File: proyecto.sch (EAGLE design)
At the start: 48 parts, among them IC1 ADE9153AACPZ, J1 796638-3, K1 PR28-3V-360-1A-E, Q1 12.288M, Q2 BSS123, U1 ESP32-PICO-MINI-02-N8R2ESP32-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

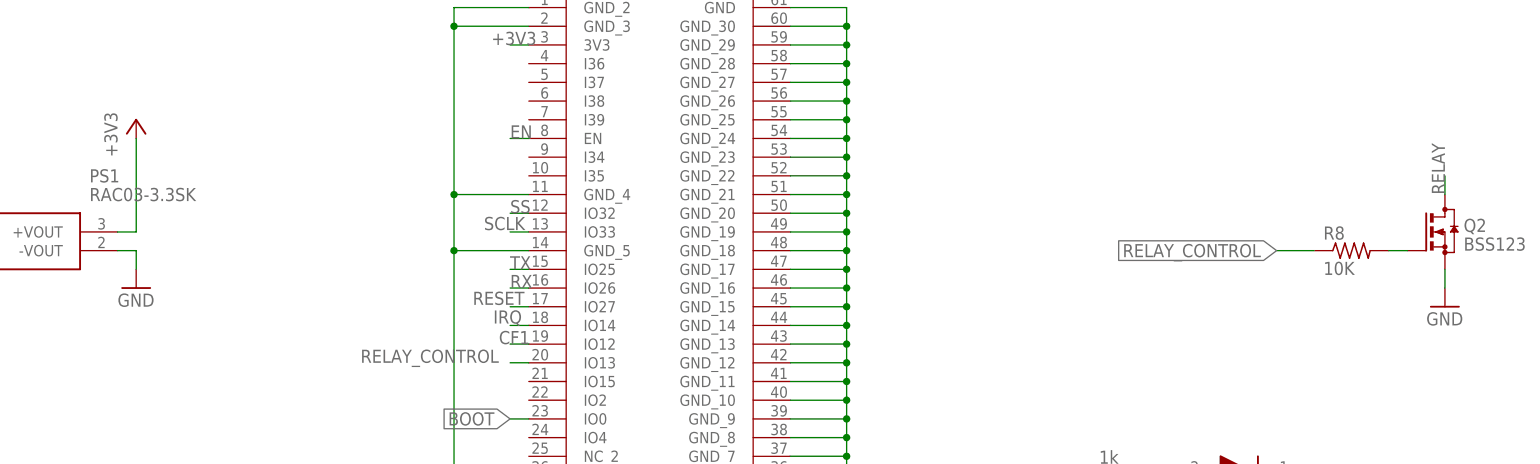
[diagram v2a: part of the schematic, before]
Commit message: Se añadieron test pads
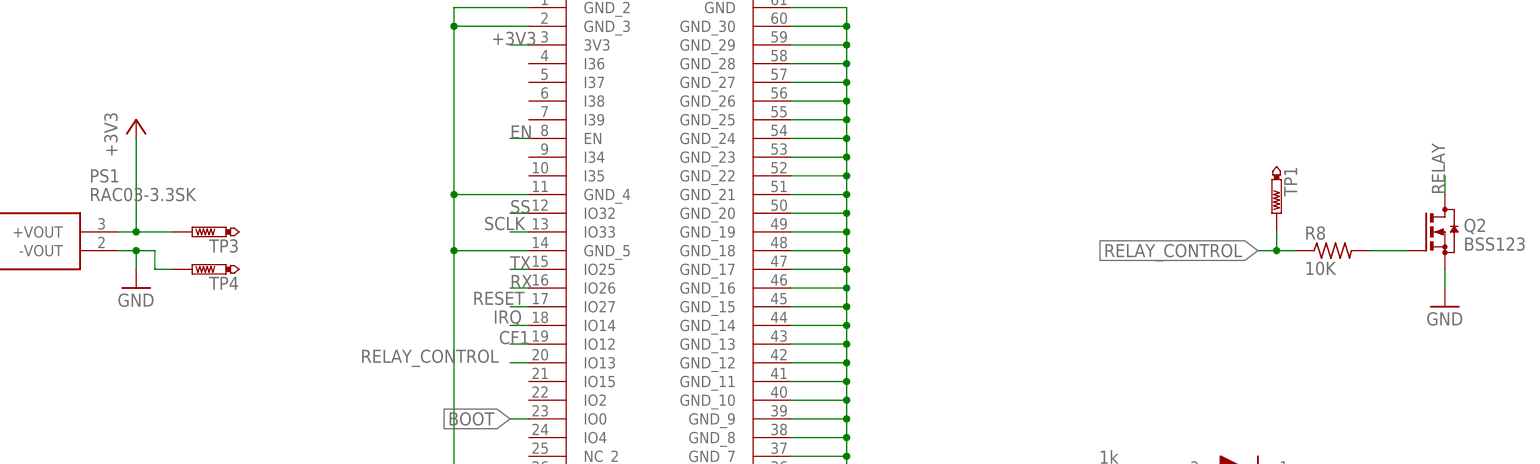
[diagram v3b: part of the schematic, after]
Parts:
- added TP1, TP3, TP4: PTR1TP10R, testpad:PTR1TP10R
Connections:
- net +3V3: now also TP3.TP
- net GND: now also TP4.TP
- net RELAY_CONTROL: now also TP1.TP
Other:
- moved on the sheet: R8
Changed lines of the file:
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@@
 <part name="LED3" library="libreria_propia" deviceset="NCD0805G1" device=""/>
 <part name="R12" library="rcl" library_urn="urn:adsk.eagle:library:334" deviceset="R-US_" device="R0402" package3d_urn="urn:adsk.eagle:package:23547/3" value="1k"/>
+<part name="TP3" library="testpad" library_urn="urn:adsk.eagle:library:385" deviceset="PTR1" device="TP10R" package3d_urn="urn:adsk.eagle:package:27959/1" value="PTR1TP10R"/>
+<part name="TP4" library="testpad" library_urn="urn:adsk.eagle:library:385" deviceset="PTR1" device="TP10R" package3d_urn="urn:adsk.eagle:package:27959/1" value="PTR1TP10R"/>
+<part name="TP1" library="testpad" library_urn="urn:adsk.eagle:library:385" deviceset="PTR1" device="TP10R" package3d_urn="urn:adsk.eagle:package:27959/1"/>
 </parts>
 <sheets>
@@
 <attribute name="VALUE" x="233.68" y="99.06" size="1.778" layer="96"/>
 </instance>
-<instance part="R8" gate="G$1" x="223.52" y="109.22" smashed="yes">
-<attribute name="NAME" x="219.71" y="110.7186" size="1.778" layer="95"/>
-<attribute name="VALUE" x="219.71" y="105.918" size="1.778" layer="96"/>
+<instance part="R8" gate="G$1" x="220.98" y="109.22" smashed="yes">
+<attribute name="NAME" x="217.17" y="110.7186" size="1.778" layer="95"/>
+<attribute name="VALUE" x="217.17" y="105.918" size="1.778" layer="96"/>
 </instance>
 <instance part="C23" gate="G$1" x="38.1" y="14.224" smashed="yes">
@@
 <attribute name="NAME" x="189.23" y="77.2414" size="1.778" layer="95" rot="MR180"/>
 <attribute name="VALUE" x="189.23" y="82.042" size="1.778" layer="96" rot="MR180"/>
+</instance>
+<instance part="TP3" gate="G$1" x="66.04" y="111.76" smashed="yes" rot="R90">
+<attribute name="NAME" x="72.39" y="110.744" size="1.778" layer="95" rot="R180"/>
+<attribute name="TP_SIGNAL_NAME" x="68.58" y="113.03" size="1.778" layer="97" rot="R90"/>
+</instance>
+<instance part="TP4" gate="G$1" x="66.04" y="106.68" smashed="yes" rot="R90">
+<attribute name="NAME" x="72.39" y="105.664" size="1.778" layer="95" rot="R180"/>
+<attribute name="TP_SIGNAL_NAME" x="68.58" y="107.95" size="1.778" layer="97" rot="R90"/>
+</instance>
+<instance part="TP1" gate="G$1" x="213.36" y="114.3" smashed="yes" rot="R180">
+<attribute name="NAME" x="214.376" y="120.65" size="1.778" layer="95" rot="R270"/>
+<attribute name="TP_SIGNAL_NAME" x="212.09" y="116.84" size="1.778" layer="97" rot="R180"/>
 </instance>
 </instances>
@@
 <pinref part="GND12" gate="1" pin="GND"/>
 <wire x1="58.42" y1="106.68" x2="58.42" y2="109.22" width="0.1524" layer="91"/>
+<pinref part="TP4" gate="G$1" pin="TP"/>
+<wire x1="63.5" y1="106.68" x2="60.96" y2="106.68" width="0.1524" layer="91"/>
+<wire x1="60.96" y1="106.68" x2="60.96" y2="109.22" width="0.1524" layer="91"/>
+<wire x1="60.96" y1="109.22" x2="58.42" y2="109.22" width="0.1524" layer="91"/>
+<junction x="58.42" y="109.22"/>
 </segment>
 </net>
@@
 <pinref part="+3V1" gate="G$1" pin="+3V3"/>
 <wire x1="58.42" y1="111.76" x2="58.42" y2="124.46" width="0.1524" layer="91"/>
+<pinref part="TP3" gate="G$1" pin="TP"/>
+<wire x1="63.5" y1="111.76" x2="58.42" y2="111.76" width="0.1524" layer="91"/>
+<junction x="58.42" y="111.76"/>
 </segment>
 <segment>
@@
 </segment>
 </net>
-<net name="N$13" class="0">
-<segment>
-<pinref part="R8" gate="G$1" pin="2"/>
-<pinref part="Q2" gate="G$1" pin="G"/>
-<wire x1="228.6" y1="109.22" x2="231.14" y2="109.22" width="0.1524" layer="91"/>
-</segment>
-</net>
 <net name="RELAY_CONTROL" class="0">
 <segment>
 <pinref part="R8" gate="G$1" pin="1"/>
-<label x="213.36" y="109.22" size="1.778" layer="95" rot="R180" xref="yes"/>
-<wire x1="218.44" y1="109.22" x2="213.36" y2="109.22" width="0.1524" layer="91"/>
+<label x="210.82" y="109.22" size="1.778" layer="95" rot="R180" xref="yes"/>
+<wire x1="215.9" y1="109.22" x2="213.36" y2="109.22" width="0.1524" layer="91"/>
+<pinref part="TP1" gate="G$1" pin="TP"/>
+<wire x1="213.36" y1="109.22" x2="210.82" y2="109.22" width="0.1524" layer="91"/>
+<wire x1="213.36" y1="111.76" x2="213.36" y2="109.22" width="0.1524" layer="91"/>
+<junction x="213.36" y="109.22"/>
 </segment>
 <segment>
@@
 </segment>
 </net>
+<net name="N$13" class="0">
+<segment>
+<pinref part="R8" gate="G$1" pin="2"/>
+<pinref part="Q2" gate="G$1" pin="G"/>
+<wire x1="226.06" y1="109.22" x2="231.14" y2="109.22" width="0.1524" layer="91"/>
+</segment>
+</net>

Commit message: Finalizado
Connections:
- net MONDA renamed CARGA-M
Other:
- note added: "1/2"
- note added: "2/2"
- note added: "CIRCUITO DE POTENCIA EN ESTA PARTE SE UBICA EL MEDIDOR DE ENERGIA CON SU CIRCUITO ESPECIFICADO EN EL DATASHEET, TAMBIEN ESTA EL RELE DEL CONTROL DE LA CARGA Y LA BORNERA HACIA LA CARGA"
- note added: "JUAN ANDRES ABELLA BALLEN"
- note added: "JUAN ANDRES RODRIGUEZ RUIZ"
- note added: "MEDIDOR DE VARIABLES ELECTRICAS"
- note added: "PARTE DE BAJA POTENCIA EN ESTA PARTE ESTA EL CIRCUITO DEL MICROCONTROLADOR, FUENTE DE PODER Y EL SISTEMA DE CONTROL DE RELE"
- note added: "PROYECTO IDIE"
- note added: "TOMAS FELIPE MONTAÑEZ PIÑEROS"
- note removed: "1.0"
- note removed: "LOS MAS ASPEROS"
- moved on the sheet: C17, C18, C19, C20, C21, C22, C23, D1, IC1, J1, K1, LED1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

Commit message: Adicion de pistas faltantes
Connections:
- new net CF2: IC1.ZX/DREADY/CF2, U1.IO13
- new net N$16: IC1.IBN, IC1.IBP
- net GND: now also IC1.IBMS
- net N$2: now also IC1.IAMS
- net RELAY_CONTROL: now also U1.IO15; no longer U1.IO13

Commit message: .
.
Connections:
- net CARGA renamed M
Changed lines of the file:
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@@
 </segment>
 </net>
-<net name="CARGA" class="0">
+<net name="M" class="0">
 <segment>
 <pinref part="J1" gate="G$1" pin="1"/>

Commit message: XDIN
XDIN
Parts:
- removed Q1: 12.288M, crystal-geyer_V1_0:KX-5
- added Y1: NX3225GA-12.288M-STD-CRG-2, SamacSys_Parts:NX3225GA-12.288M-STD-CRG-2
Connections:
- net CLKIN: now also Y1.CRYSTAL_1; no longer Q1.1
- net CLKOUT: now also Y1.CRYSTAL_2; no longer Q1.2
- net GND: now also Y1.GND_1, Y1.GND_2
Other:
- moved on the sheet: C15, C16
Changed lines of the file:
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@@
 <part name="C12" library="rcl" library_urn="urn:adsk.eagle:library:334" deviceset="C-EU" device="C0402K" package3d_urn="urn:adsk.eagle:package:23679/2" value="4.7u"/>
 <part name="GND9" library="supply1" library_urn="urn:adsk.eagle:library:371" deviceset="GND" device=""/>
-<part name="Q1" library="crystal-geyer_V1_0" library_urn="urn:adsk.eagle:library:203" deviceset="KX" device="-5" package3d_urn="urn:adsk.eagle:package:11926/1" value="12.288M"/>
 <part name="C13" library="rcl" library_urn="urn:adsk.eagle:library:334" deviceset="C-EU" device="C0402K" package3d_urn="urn:adsk.eagle:package:23679/2" value="0.1u"/>
 <part name="C14" library="rcl" library_urn="urn:adsk.eagle:library:334" deviceset="C-EU" device="C0402K" package3d_urn="urn:adsk.eagle:package:23679/2" value="4.7u"/>
@@
 <part name="TP4" library="testpad" library_urn="urn:adsk.eagle:library:385" deviceset="PTR1" device="TP10R" package3d_urn="urn:adsk.eagle:package:27959/1" value="PTR1TP10R"/>
 <part name="TP1" library="testpad" library_urn="urn:adsk.eagle:library:385" deviceset="PTR1" device="TP10R" package3d_urn="urn:adsk.eagle:package:27959/1"/>
+<part name="Y1" library="SamacSys_Parts" deviceset="NX3225GA-12.288M-STD-CRG-2" device=""/>
+<part name="GND20" library="supply1" library_urn="urn:adsk.eagle:library:371" deviceset="GND" device=""/>
+<part name="GND21" library="supply1" library_urn="urn:adsk.eagle:library:371" deviceset="GND" device=""/>
 </parts>
 <sheets>
@@
 <attribute name="VALUE" x="332.74" y="7.62" size="1.778" layer="96"/>
 </instance>
-<instance part="Q1" gate="G$1" x="374.65" y="19.812" smashed="yes" rot="R90">
-<attribute name="NAME" x="373.38" y="23.622" size="1.778" layer="95" rot="R180"/>
-<attribute name="VALUE" x="377.19" y="23.622" size="1.778" layer="96" rot="R270"/>
-</instance>
 <instance part="C13" gate="G$1" x="363.22" y="20.32" smashed="yes">
 <attribute name="NAME" x="364.744" y="20.701" size="1.778" layer="95"/>
@@
 <attribute name="VALUE" x="350.52" y="7.62" size="1.778" layer="96"/>
 </instance>
-<instance part="C15" gate="G$1" x="382.27" y="24.892" smashed="yes">
-<attribute name="NAME" x="383.794" y="25.273" size="1.778" layer="95"/>
-<attribute name="VALUE" x="383.794" y="20.193" size="1.778" layer="96"/>
-</instance>
-<instance part="C16" gate="G$1" x="382.27" y="14.732" smashed="yes">
-<attribute name="NAME" x="383.794" y="15.113" size="1.778" layer="95"/>
-<attribute name="VALUE" x="383.794" y="10.033" size="1.778" layer="96"/>
-</instance>
-<instance part="GND11" gate="1" x="387.35" y="7.112" smashed="yes">
-<attribute name="VALUE" x="384.81" y="4.572" size="1.778" layer="96"/>
+<instance part="C15" gate="G$1" x="504.19" y="151.892" smashed="yes">
+<attribute name="NAME" x="505.714" y="152.273" size="1.778" layer="95"/>
+<attribute name="VALUE" x="505.714" y="147.193" size="1.778" layer="96"/>
+</instance>
+<instance part="C16" gate="G$1" x="504.19" y="141.732" smashed="yes">
+<attribute name="NAME" x="505.714" y="142.113" size="1.778" layer="95"/>
+<attribute name="VALUE" x="505.714" y="137.033" size="1.778" layer="96"/>
+</instance>
+<instance part="GND11" gate="1" x="509.27" y="134.112" smashed="yes">
+<attribute name="VALUE" x="506.73" y="131.572" size="1.778" layer="96"/>
 </instance>
 <instance part="+3V1" gate="G$1" x="150.876" y="119.634" smashed="yes">
@@
 <attribute name="NAME" x="153.924" y="77.724" size="1.778" layer="95" rot="R270"/>
 <attribute name="TP_SIGNAL_NAME" x="151.638" y="73.914" size="1.778" layer="97" rot="R180"/>
+</instance>
+<instance part="Y1" gate="G$1" x="436.88" y="157.48" smashed="yes">
+<attribute name="NAME" x="473.71" y="165.1" size="1.778" layer="95" align="center-left"/>
+<attribute name="VALUE" x="473.71" y="162.56" size="1.778" layer="96" align="center-left"/>
+</instance>
+<instance part="GND20" gate="1" x="480.06" y="149.86" smashed="yes">
+<attribute name="VALUE" x="477.52" y="147.32" size="1.778" layer="96"/>
+</instance>
+<instance part="GND21" gate="1" x="434.34" y="162.56" smashed="yes" rot="R180">
+<attribute name="VALUE" x="436.88" y="165.1" size="1.778" layer="96" rot="R180"/>
 </instance>
 </instances>
@@
 <segment>
 <pinref part="GND11" gate="1" pin="GND"/>
-<wire x1="387.35" y1="9.652" x2="387.35" y2="17.272" width="0.1524" layer="91"/>
+<wire x1="509.27" y1="136.652" x2="509.27" y2="144.272" width="0.1524" layer="91"/>
 <pinref part="C16" gate="G$1" pin="1"/>
 <pinref part="C15" gate="G$1" pin="2"/>
-<wire x1="382.27" y1="17.272" x2="382.27" y2="19.812" width="0.1524" layer="91"/>
-<wire x1="387.35" y1="17.272" x2="382.27" y2="17.272" width="0.1524" layer="91"/>
-<junction x="382.27" y="17.272"/>
+<wire x1="504.19" y1="144.272" x2="504.19" y2="146.812" width="0.1524" layer="91"/>
+<wire x1="509.27" y1="144.272" x2="504.19" y2="144.272" width="0.1524" layer="91"/>
+<junction x="504.19" y="144.272"/>
 </segment>
 <segment>
@@
 <junction x="150.876" y="101.854"/>
 </segment>
+<segment>
+<pinref part="GND20" gate="1" pin="GND"/>
+<wire x1="480.06" y1="152.4" x2="480.06" y2="154.94" width="0.1524" layer="91"/>
+<pinref part="Y1" gate="G$1" pin="GND_1"/>
+<wire x1="480.06" y1="154.94" x2="477.52" y2="154.94" width="0.1524" layer="91"/>
+</segment>
+<segment>
+<pinref part="Y1" gate="G$1" pin="GND_2"/>
+<pinref part="GND21" gate="1" pin="GND"/>
+<wire x1="436.88" y1="157.48" x2="434.34" y2="157.48" width="0.1524" layer="91"/>
+<wire x1="434.34" y1="157.48" x2="434.34" y2="160.02" width="0.1524" layer="91"/>
+</segment>
 </net>
 <net name="AVDDOUT" class="0">
@@
 </segment>
 <segment>
-<pinref part="Q1" gate="G$1" pin="2"/>
-<wire x1="374.65" y1="22.352" x2="374.65" y2="27.432" width="0.1524" layer="91"/>
 <pinref part="C15" gate="G$1" pin="1"/>
-<wire x1="374.65" y1="27.432" x2="382.27" y2="27.432" width="0.1524" layer="91"/>
-<label x="373.38" y="27.94" size="1.778" layer="95"/>
+<label x="495.3" y="154.94" size="1.778" layer="95"/>
+<pinref part="Y1" gate="G$1" pin="CRYSTAL_2"/>
+<wire x1="504.19" y1="154.432" x2="504.19" y2="157.48" width="0.1524" layer="91"/>
+<wire x1="504.19" y1="157.48" x2="477.52" y2="157.48" width="0.1524" layer="91"/>
 </segment>
 </net>
@@
 <segment>
 <pinref part="C16" gate="G$1" pin="2"/>
-<pinref part="Q1" gate="G$1" pin="1"/>
-<wire x1="374.65" y1="17.272" x2="374.65" y2="9.652" width="0.1524" layer="91"/>
-<wire x1="374.65" y1="9.652" x2="382.27" y2="9.652" width="0.1524" layer="91"/>
-<label x="374.142" y="7.874" size="1.778" layer="95"/>
-</segment>
-</net>
+<wire x1="496.57" y1="136.652" x2="504.19" y2="136.652" width="0.1524" layer="91"/>
+<label x="496.062" y="134.874" size="1.778" layer="95"/>
+<wire x1="504.19" y1="136.652" x2="441.96" y2="136.652" width="0.1524" layer="91"/>
+<junction x="504.19" y="136.652"/>
+<wire x1="441.96" y1="136.652" x2="441.96" y2="149.86" width="0.1524" layer="91"/>
+<wire x1="441.96" y1="149.86" x2="434.34" y2="149.86" width="0.1524" layer="91"/>
+<pinref part="Y1" gate="G$1" pin="CRYSTAL_1"/>
+<wire x1="434.34" y1="149.86" x2="434.34" y2="154.94" width="0.1524" layer="91"/>
+<wire x1="434.34" y1="154.94" x2="436.88" y2="154.94" width="0.1524" layer="91"/>
+</segment>
+</net>
